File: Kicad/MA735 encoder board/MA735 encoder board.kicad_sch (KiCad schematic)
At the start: 4 parts, among them J1 FPC contacts 0.3mm, U1 MA735GGU-Z

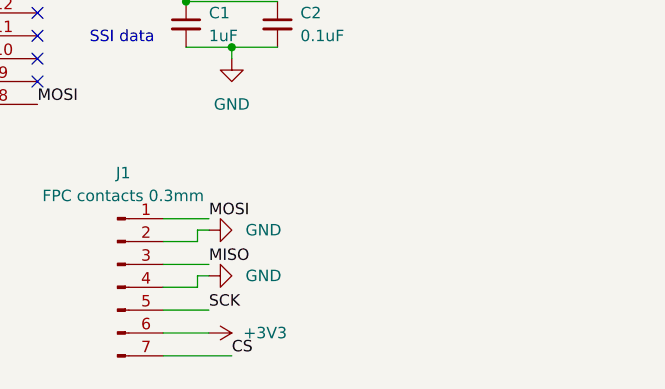
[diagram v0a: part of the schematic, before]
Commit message: Finished Magnetic encoder flex pcb
I added a hatched ground plane. I also re-arranged the filter capacitors so the clock signal could get out without needing vias. There is much more room now with the wiring
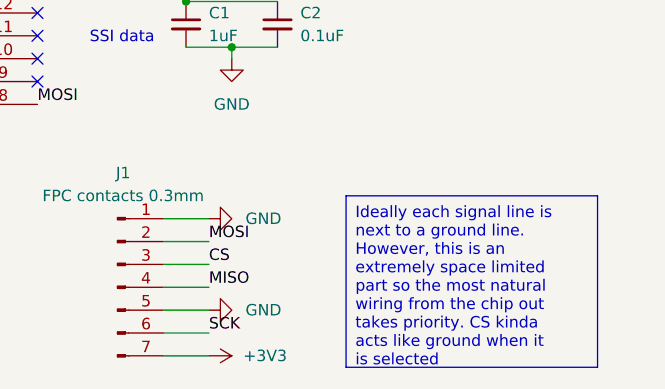
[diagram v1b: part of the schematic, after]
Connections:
- net +3V3: now also J1.7 (Pin_7); no longer J1.6 (Pin_6)
- net CS: now also J1.3 (Pin_3); no longer J1.7 (Pin_7)
- net GND: now also J1.1 (Pin_1), J1.5 (Pin_5); no longer J1.2 (Pin_2), J1.4 (Pin_4)
- net MISO: now also J1.4 (Pin_4); no longer J1.3 (Pin_3)
- net MOSI: now also J1.2 (Pin_2); no longer J1.1 (Pin_1)
- net SCK: now also J1.6 (Pin_6); no longer J1.5 (Pin_5)
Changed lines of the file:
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@@
 	(wire
 		(pts
-			(xy 182.88 120.65) (xy 175.26 120.65)
-		)
-		(stroke
-			(width 0)
-			(type default)
-		)
-	)
-	(wire
-		(pts
-			(xy 179.07 111.76) (xy 179.07 113.03)
+			(xy 180.34 120.65) (xy 175.26 120.65)
 		)
 		(stroke
@@
 	(wire
 		(pts
-			(xy 180.34 106.68) (xy 179.07 106.68)
-		)
-		(stroke
-			(width 0)
-			(type default)
-		)
-	)
-	(wire
-		(pts
 			(xy 110.49 85.09) (xy 110.49 86.36)
 		)
@@
 	(wire
 		(pts
-			(xy 179.07 113.03) (xy 175.26 113.03)
+			(xy 175.26 113.03) (xy 180.34 113.03)
 		)
 		(stroke
@@
 	(wire
 		(pts
-			(xy 179.07 107.95) (xy 175.26 107.95)
+			(xy 175.26 107.95) (xy 180.34 107.95)
 		)
 		(stroke
@@
 	(wire
 		(pts
-			(xy 179.07 106.68) (xy 179.07 107.95)
-		)
-		(stroke
-			(width 0)
-			(type default)
-		)
-	)
-	(wire
-		(pts
 			(xy 182.88 86.36) (xy 187.96 86.36)
 		)
@@
 		)
 	)
-	(wire
-		(pts
-			(xy 180.34 111.76) (xy 179.07 111.76)
-		)
-		(stroke
-			(width 0)
-			(type default)
+	(text_box "Ideally each signal line is next to a ground line. However, this is an extremely space limited part so the most natural wiring from the chip out takes priority. CS kinda acts like ground when it is selected"
+		(exclude_from_sim no)
+		(at 195.58 102.87 0)
+		(size 27.94 19.05)
+		(stroke
+			(width 0)
+			(type default)
+		)
+		(fill
+			(type none)
+		)
+		(effects
+			(font
+				(size 1.27 1.27)
+			)
+			(justify left top)
 		)
 	)
@@
 	)
 	(label "MOSI"
-		(at 180.34 105.41 0)
+		(at 180.34 107.95 0)
 		(fields_autoplaced yes)
 		(effects
@@
 	)
 	(label "MISO"
-		(at 180.34 110.49 0)
+		(at 180.34 113.03 0)
 		(fields_autoplaced yes)
 		(effects
@@
 	)
 	(label "CS"
-		(at 182.88 120.65 0)
+		(at 180.34 110.49 0)
 		(fields_autoplaced yes)
 		(effects
@@
 	)
 	(label "SCK"
-		(at 180.34 115.57 0)
+		(at 180.34 118.11 0)
 		(fields_autoplaced yes)
 		(effects
@@
 	(symbol
 		(lib_id "power:GND")
-		(at 180.34 111.76 90)
+		(at 180.34 115.57 90)
 		(unit 1)
 		(exclude_from_sim no)
@@
 		(fields_autoplaced yes)
 		(property "Reference" "#PWR04"
-			(at 186.69 111.76 0)
+			(at 186.69 115.57 0)
 			(effects
 				(font
@@
 		)
 		(property "Value" "GND"
-			(at 184.404 111.7601 90)
+			(at 184.404 115.5701 90)
 			(effects
 				(font
@@
 		)
 		(property "Footprint" ""
-			(at 180.34 111.76 0)
+			(at 180.34 115.57 0)
 			(effects
 				(font
@@
 		)
 		(property "Datasheet" ""
-			(at 180.34 111.76 0)
+			(at 180.34 115.57 0)
 			(effects
 				(font
@@
 		)
 		(property "Description" "Power symbol creates a global label with name \"GND\" , ground"
-			(at 180.34 111.76 0)
+			(at 180.34 115.57 0)
 			(effects
 				(font
@@
 	(symbol
 		(lib_id "power:+3V3")
-		(at 180.34 118.11 270)
+		(at 180.34 120.65 270)
 		(unit 1)
 		(exclude_from_sim no)
@@
 		(fields_autoplaced yes)
 		(property "Reference" "#PWR07"
-			(at 176.53 118.11 0)
+			(at 176.53 120.65 0)
 			(effects
 				(font
@@
 		)
 		(property "Value" "+3V3"
-			(at 184.15 118.1101 90)
+			(at 184.15 120.6501 90)
 			(effects
 				(font
@@
 		)
 		(property "Footprint" ""
-			(at 180.34 118.11 0)
+			(at 180.34 120.65 0)
 			(effects
 				(font
@@
 		)
 		(property "Datasheet" ""
-			(at 180.34 118.11 0)
+			(at 180.34 120.65 0)
 			(effects
 				(font
@@
 		)
 		(property "Description" "Power symbol creates a global label with name \"+3V3\""
-			(at 180.34 118.11 0)
+			(at 180.34 120.65 0)
 			(effects
 				(font
@@
 	(symbol
 		(lib_id "power:GND")
-		(at 180.34 106.68 90)
+		(at 180.34 105.41 90)
 		(unit 1)
 		(exclude_from_sim no)
@@
 		(fields_autoplaced yes)
 		(property "Reference" "#PWR05"
-			(at 186.69 106.68 0)
+			(at 186.69 105.41 0)
 			(effects
 				(font
@@
 		)
 		(property "Value" "GND"
-			(at 184.404 106.6801 90)
+			(at 184.404 105.4101 90)
 			(effects
 				(font
@@
 		)
 		(property "Footprint" ""
-			(at 180.34 106.68 0)
+			(at 180.34 105.41 0)
 			(effects
 				(font
@@
 		)
 		(property "Datasheet" ""
-			(at 180.34 106.68 0)
+			(at 180.34 105.41 0)
 			(effects
 				(font
@@
 		)
 		(property "Description" "Power symbol creates a global label with name \"GND\" , ground"
-			(at 180.34 106.68 0)
-			(effects
-				(font
+			(at 180.34 105.41 0)
+			(effects
+				(font

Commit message: Gerbers and BOM for v0.4 PCB
I adjusted all the testpoints to be excluded from the BOM.
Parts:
- J1: now left out of the parts list
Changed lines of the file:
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@@
 		(unit 1)
 		(exclude_from_sim no)
-		(in_bom yes)
+		(in_bom no)
 		(on_board yes)
 		(dnp no)
